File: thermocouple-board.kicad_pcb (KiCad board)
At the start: 2 copper layers, 72 parts, among them J1 Programming Header, J2 RJ45_Amphenol_RJMG1BD3B8K1ANR, J3 Conn_01x02, SW1 RESET, U1 ATSAME51J20A-A, U10 ENC28J60x-SO, U11 MC33063AD, U2 MCP9601_ZM, U3 MCP9601_ZM, U4 MCP9601_ZM, U5 MCP9601_ZM, U6 MCP9601_ZM, U7 MCP9601_ZM, U8 MCP9601_ZM, U9 MCP9601_ZM, Y1 25MHz

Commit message: Begin PCB placement and routing
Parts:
- added J10: TC7, Connector_PinHeader_2.54mm:PinHeader_1x02_P2.54mm_Vertical, F.Cu at (223.6, 71.6)
- added J11: TC8, Connector_PinHeader_2.54mm:PinHeader_1x02_P2.54mm_Vertical, F.Cu at (213.5, 71.6)
- added J4: TC1, Connector_PinHeader_2.54mm:PinHeader_1x02_P2.54mm_Vertical, F.Cu at (284.0, 71.6)
- added J5: TC2, Connector_PinHeader_2.54mm:PinHeader_1x02_P2.54mm_Vertical, F.Cu at (273.9, 71.6)
- added J6: TC3, Connector_PinHeader_2.54mm:PinHeader_1x02_P2.54mm_Vertical, F.Cu at (263.8, 71.6)
- added J7: TC4, Connector_PinHeader_2.54mm:PinHeader_1x02_P2.54mm_Vertical, F.Cu at (253.8, 71.6)
- added J8: TC5, Connector_PinHeader_2.54mm:PinHeader_1x02_P2.54mm_Vertical, F.Cu at (243.7, 71.6)
- added J9: TC6, Connector_PinHeader_2.54mm:PinHeader_1x02_P2.54mm_Vertical, F.Cu at (233.6, 71.6)
- moved J2 253.9 mm to (276.2, 119.4), turned to 90 degrees
- moved C17 246.9 mm to (279.4, 129.5), turned to 90 degrees
- moved C16 230.5 mm to (269.9, 133.3), turned to 90 degrees
- moved Y1 226.2 mm to (252.7, 103.5), turned to 180 degrees
- moved R23 225.4 mm to (285.8, 129.5), turned to 270 degrees
- moved C8 222.0 mm to (266.7, 102.9), turned to 270 degrees
- moved C9 218.5 mm to (263.5, 102.9), turned to 270 degrees
- moved R19 218.2 mm to (269.9, 101.9), turned to 270 degrees
- moved C15 216.2 mm to (273.7, 95.2), turned to 270 degrees
- moved R20 215.2 mm to (273.7, 101.9), turned to 270 degrees
- moved U10 210.9 mm to (255.3, 114.3), turned to 90 degrees
- moved R18 210.8 mm to (269.1, 124.8), turned to 270 degrees
- moved R22 209.9 mm to (264.4, 126.9), turned to 180 degrees
- moved C7 209.9 mm to (259.7, 125.1), turned to 270 degrees
- moved R24 208.1 mm to (278.1, 95.2), turned to 90 degrees
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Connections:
- U2 pad 15: GND -> Net-(U2-Pad15)
- U2 pad 16: (no net) -> GND
- U3 pad 15: /Thermocouples/ADDR_2 -> /Thermocouples/TEST
- U3 pad 16: (no net) -> /Thermocouples/ADDR_2
- U4 pad 15: /Thermocouples/ADDR_3 -> Net-(U4-Pad15)
- U4 pad 16: (no net) -> /Thermocouples/ADDR_3
- U5 pad 15: /Thermocouples/ADDR_4 -> Net-(U5-Pad15)
- U5 pad 16: (no net) -> /Thermocouples/ADDR_4
- U6 pad 15: /Thermocouples/ADDR_5 -> Net-(U6-Pad15)
- U6 pad 16: (no net) -> /Thermocouples/ADDR_5
- U7 pad 16: (no net) -> /Thermocouples/ADDR_6
- U8 pad 15: /Thermocouples/ADDR_7 -> Net-(U8-Pad15)
- U8 pad 16: (no net) -> /Thermocouples/ADDR_7
- U9 pad 15: +3V3 -> Net-(U9-Pad15)
- U9 pad 16: (no net) -> +3V3
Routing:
- net /Thermocouples/SCL: track 0.00 -> 146.2 mm, vias 0 -> 9
- net /Thermocouples/SDA: track 0.00 -> 141.2 mm, vias 0 -> 9
- net +3V3: track 0.00 -> 45.1 mm
- net Net-(R27-Pad2): track 0.00 -> 30.3 mm
- net /MCU/SWDIO: track 0.00 -> 22.0 mm
- net RESET: track 0.00 -> 20.4 mm
- net Net-(C17-Pad2): track 0.00 -> 20.3 mm
- net Net-(J2-PadL2): track 0.00 -> 18.8 mm
- net /Ethernet/TPOUT+: track 0.00 -> 17.8 mm
- net /Ethernet/TPOUT-: track 0.00 -> 12.9 mm
- net Net-(C13-Pad1): track 0.00 -> 12.5 mm
- net Net-(C12-Pad1): track 0.00 -> 12.5 mm
- net Net-(C16-Pad2): track 0.00 -> 10.3 mm
- net Net-(J2-PadL3): track 0.00 -> 9.41 mm
- net /Ethernet/TPIN-: track 0.00 -> 9.14 mm
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
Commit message: Add PDF schematics
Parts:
- J1: footprint Connector_PinSocket_2.54mm:PinSocket_2x05_P2.54mm_Vertical -> Connector_PinHeader_2.54mm:PinHeader_2x05_P2.54mm_Vertical
- moved R32 10.4 mm to (269.9, 146.7), turned to 270 degrees
- moved C18 8.53 mm to (211.7, 123.1), turned to 0 degrees
- moved R26 5.09 mm to (275.0, 142.6)
- moved R19 4.45 mm to (274.3, 101.9)
- moved R20 3.18 mm to (270.5, 101.9)
- moved R14 0.43 mm to (256.3, 125.1)
- moved R15 0.43 mm to (253.8, 125.1)
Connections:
- net /Thermocouples/TC_NEGATIVE_1 renamed /Thermocouples/TC1-
- net /Thermocouples/TC_NEGATIVE_2 renamed /Thermocouples/TC2-
- net /Thermocouples/TC_NEGATIVE_3 renamed /Thermocouples/TC3-
- net /Thermocouples/TC_NEGATIVE_4 renamed /Thermocouples/TC4-
- net /Thermocouples/TC_NEGATIVE_5 renamed /Thermocouples/TC5-
- net /Thermocouples/TC_NEGATIVE_6 renamed /Thermocouples/TC6-
- net /Thermocouples/TC_NEGATIVE_7 renamed /Thermocouples/TC7-
- net /Thermocouples/TC_NEGATIVE_8 renamed /Thermocouples/TC8-
- net /Thermocouples/TC_POSITIVE_1 renamed /Thermocouples/TC1+
- net /Thermocouples/TC_POSITIVE_2 renamed /Thermocouples/TC2+
- net /Thermocouples/TC_POSITIVE_3 renamed /Thermocouples/TC3+
- net /Thermocouples/TC_POSITIVE_4 renamed /Thermocouples/TC4+
- net /Thermocouples/TC_POSITIVE_5 renamed /Thermocouples/TC5+
- net /Thermocouples/TC_POSITIVE_6 renamed /Thermocouples/TC6+
- net /Thermocouples/TC_POSITIVE_7 renamed /Thermocouples/TC7+
- net /Thermocouples/TC_POSITIVE_8 renamed /Thermocouples/TC8+
- net /Thermocouples/TEST renamed Net-(U3-Pad15)
- C20 pad 1: Net-(C20-Pad1) -> +3V3
- J2 pad R5: Net-(J2-PadR5) -> Net-(C16-Pad2)
- L2 pad 2: Net-(C20-Pad1) -> +3V3
- R30 pad 1: Net-(C20-Pad1) -> +3V3
- U2 pad 21: (no net) -> GND
- U3 pad 21: (no net) -> GND
- U4 pad 21: (no net) -> GND
- U5 pad 21: (no net) -> GND
- U6 pad 21: (no net) -> GND
- U7 pad 21: (no net) -> GND
- U8 pad 21: (no net) -> GND
- U9 pad 21: (no net) -> GND
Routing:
- net +3V3: track 45.1 -> 438.4 mm
- net GND: track 0.00 -> 289.1 mm, vias 0 -> 6
- net /Ethernet/LEDA: track 0.00 -> 47.8 mm, vias 0 -> 1
- net /Ethernet/LEDB: track 0.00 -> 41.6 mm
- net /Ethernet/MOSI: track 0.00 -> 39.2 mm, vias 0 -> 2
- net /Ethernet/SCK: track 0.00 -> 38.6 mm, vias 0 -> 2
- net /Ethernet/MISO: track 0.00 -> 36.3 mm, vias 0 -> 2
- net Net-(C15-Pad2): track 0.00 -> 29.9 mm, vias 0 -> 1
- net /MCU/SWCLK: track 0.00 -> 25.7 mm
- net RESET: track 20.4 -> 44.8 mm, vias 0 -> 1
- net Net-(R26-Pad2): track 0.00 -> 24.3 mm
- net VCC: track 0.00 -> 23.2 mm
- net /Ethernet/TPOUT-: track 12.9 -> 34.1 mm, vias 0 -> 2
- net Net-(C16-Pad2): track 10.3 -> 31.0 mm
- net /Ethernet/TPIN-: track 9.14 -> 27.9 mm
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- added copper zone on F.Cu, net GND
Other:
- board outline added: 91.4 x 87.6 mm
- net class Power added: clearance 0.2, trace_width 0.5, via_dia 1, via_drill 0.4
- board text added: "DISOVERY TC PROTOTYPE 1 FEB 2020"
- board text added: "TC1"
- board text added: "TC2"
- board text added: "TC3"
- board text added: "TC4"
- board text added: "TC5"
- board text added: "TC6"
- board text added: "TC7"
- board text added: "TC8"

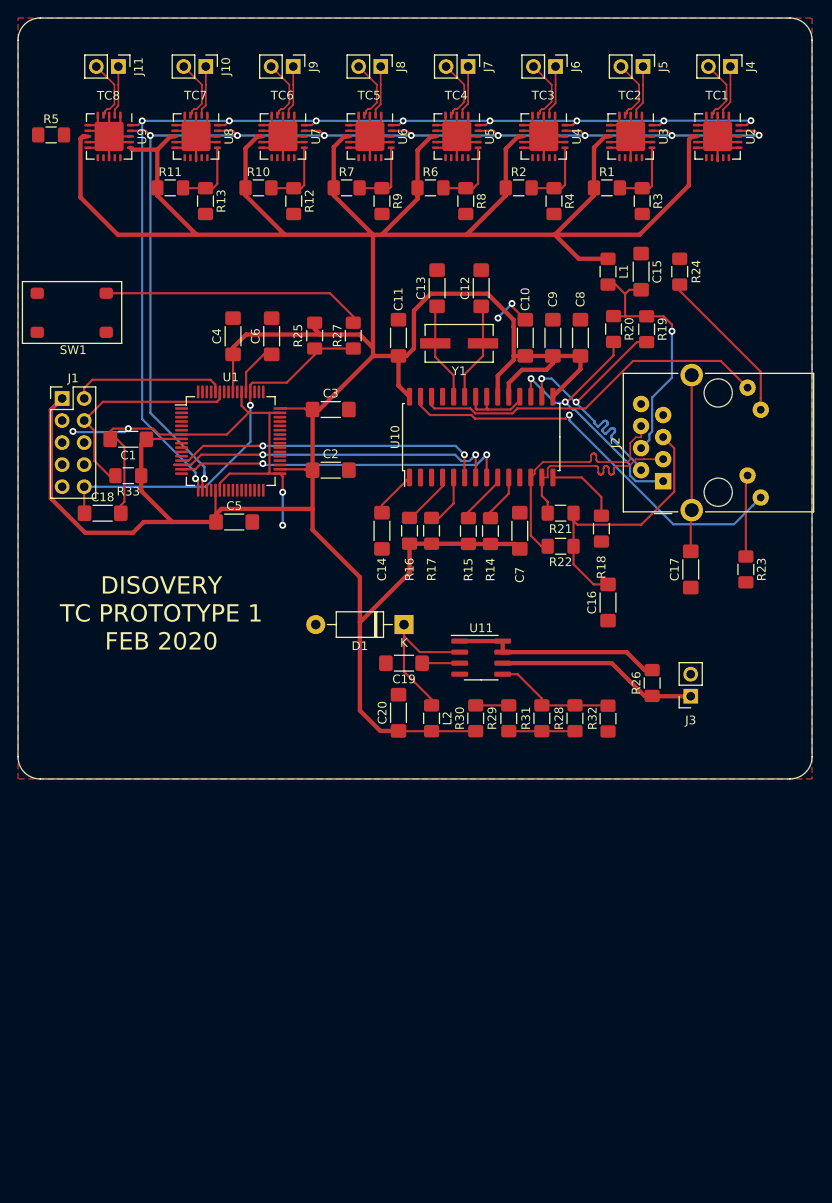
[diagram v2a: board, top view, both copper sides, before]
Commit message: Preliminary replacement of components for MCP9601
Following the changes in the previous commit, all components have been
replaced in a bid for more space efficiency to reduce costs.

No traces have been laid at this point.
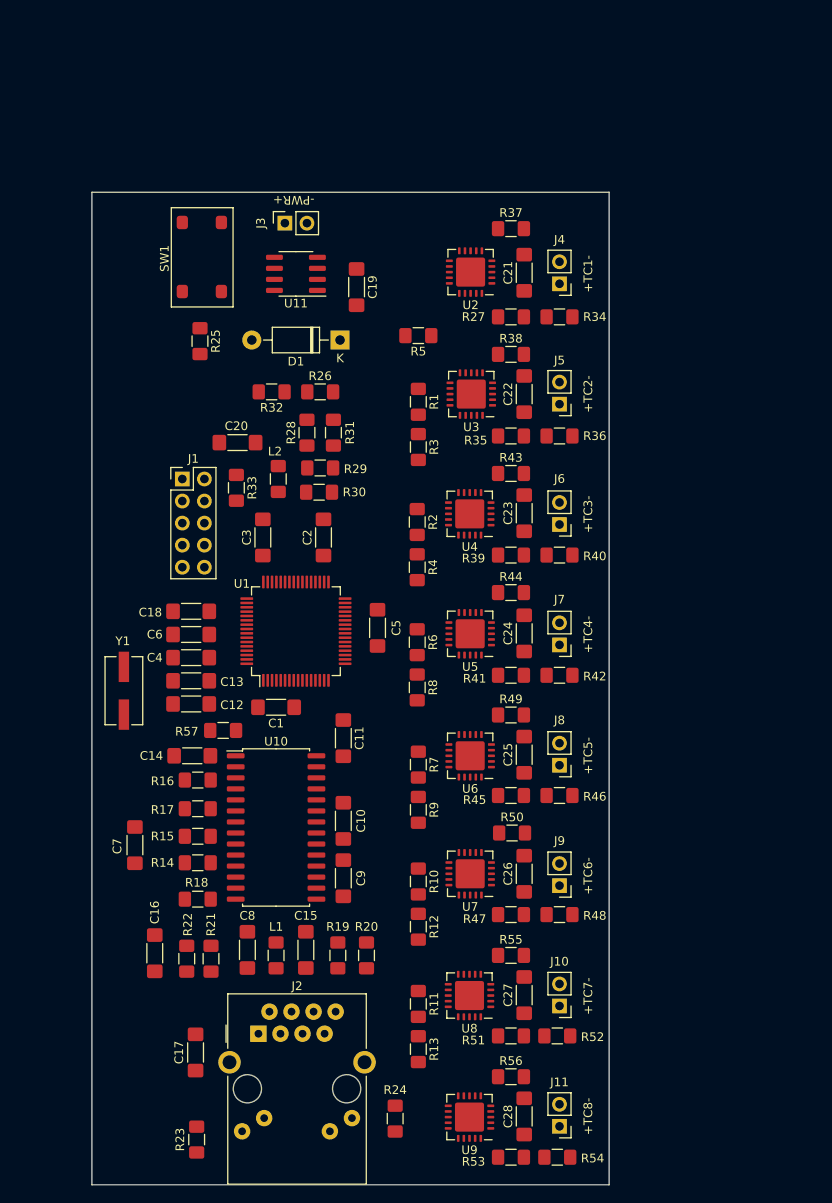
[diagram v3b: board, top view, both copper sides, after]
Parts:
- added C21: 0.1uF, Capacitor_SMD:C_1806_4516Metric_Pad1.57x1.80mm_HandSolder, F.Cu at (260.2, 95.4)
- added C22: 0.1uF, Capacitor_SMD:C_1806_4516Metric_Pad1.57x1.80mm_HandSolder, F.Cu at (260.2, 109.3)
- added C23: 0.1uF, Capacitor_SMD:C_1806_4516Metric_Pad1.57x1.80mm_HandSolder, F.Cu at (260.2, 123.1)
- added C24: 0.1uF, Capacitor_SMD:C_1806_4516Metric_Pad1.57x1.80mm_HandSolder, F.Cu at (260.2, 136.9)
- added C25: 0.1uF, Capacitor_SMD:C_1806_4516Metric_Pad1.57x1.80mm_HandSolder, F.Cu at (260.2, 150.9)
- added C26: 0.1uF, Capacitor_SMD:C_1806_4516Metric_Pad1.57x1.80mm_HandSolder, F.Cu at (260.2, 164.6)
- added C27: 0.1uF, Capacitor_SMD:C_1806_4516Metric_Pad1.57x1.80mm_HandSolder, F.Cu at (260.2, 178.6)
- added C28: 0.1uF, Capacitor_SMD:C_1806_4516Metric_Pad1.57x1.80mm_HandSolder, F.Cu at (260.2, 192.5)
- added R34: 1M, Resistor_SMD:R_1206_3216Metric_Pad1.42x1.75mm_HandSolder, F.Cu at (264.3, 100.5)
- added R35: 2M, Resistor_SMD:R_1206_3216Metric_Pad1.42x1.75mm_HandSolder, F.Cu at (258.7, 114.2)
- added R36: 1M, Resistor_SMD:R_1206_3216Metric_Pad1.42x1.75mm_HandSolder, F.Cu at (264.3, 114.2)
- added R37: 2M, Resistor_SMD:R_1206_3216Metric_Pad1.42x1.75mm_HandSolder, F.Cu at (258.7, 90.3)
- added R38: 2M, Resistor_SMD:R_1206_3216Metric_Pad1.42x1.75mm_HandSolder, F.Cu at (258.7, 104.8)
- added R39: 2M, Resistor_SMD:R_1206_3216Metric_Pad1.42x1.75mm_HandSolder, F.Cu at (258.7, 127.9)
- added R40: 1M, Resistor_SMD:R_1206_3216Metric_Pad1.42x1.75mm_HandSolder, F.Cu at (264.3, 127.9)
- added R41: 2M, Resistor_SMD:R_1206_3216Metric_Pad1.42x1.75mm_HandSolder, F.Cu at (258.7, 141.7)
- added R42: 1M, Resistor_SMD:R_1206_3216Metric_Pad1.42x1.75mm_HandSolder, F.Cu at (264.3, 141.7)
- added R43: 2M, Resistor_SMD:R_1206_3216Metric_Pad1.42x1.75mm_HandSolder, F.Cu at (258.7, 118.5)
- added R44: 2M, Resistor_SMD:R_1206_3216Metric_Pad1.42x1.75mm_HandSolder, F.Cu at (258.7, 132.2)
- added R45: 2M, Resistor_SMD:R_1206_3216Metric_Pad1.42x1.75mm_HandSolder, F.Cu at (258.7, 155.6)
- added R46: 1M, Resistor_SMD:R_1206_3216Metric_Pad1.42x1.75mm_HandSolder, F.Cu at (264.3, 155.6)
- added R47: 2M, Resistor_SMD:R_1206_3216Metric_Pad1.42x1.75mm_HandSolder, F.Cu at (258.7, 169.3)
- added R48: 1M, Resistor_SMD:R_1206_3216Metric_Pad1.42x1.75mm_HandSolder, F.Cu at (264.3, 169.3)
- added R49: 2M, Resistor_SMD:R_1206_3216Metric_Pad1.42x1.75mm_HandSolder, F.Cu at (258.7, 146.3)
- added R50: 2M, Resistor_SMD:R_1206_3216Metric_Pad1.42x1.75mm_HandSolder, F.Cu at (258.8, 159.9)
- added R51: 2M, Resistor_SMD:R_1206_3216Metric_Pad1.42x1.75mm_HandSolder, F.Cu at (258.7, 183.3)
- added R52: 1M, Resistor_SMD:R_1206_3216Metric_Pad1.42x1.75mm_HandSolder, F.Cu at (264.0, 183.3)
- added R53: 2M, Resistor_SMD:R_1206_3216Metric_Pad1.42x1.75mm_HandSolder, F.Cu at (258.7, 197.2)
- added R54: 1M, Resistor_SMD:R_1206_3216Metric_Pad1.42x1.75mm_HandSolder, F.Cu at (264.0, 197.2)
- added R55: 2M, Resistor_SMD:R_1206_3216Metric_Pad1.42x1.75mm_HandSolder, F.Cu at (258.7, 174.0)
- added R56: 2M, Resistor_SMD:R_1206_3216Metric_Pad1.42x1.75mm_HandSolder, F.Cu at (258.7, 188.0)
- added R57: 5M, Resistor_SMD:R_1206_3216Metric_Pad1.42x1.75mm_HandSolder, F.Cu at (225.6, 148.1)
- R25: value 27K -> 330
- R27: value 820 -> 2M
- R33: value 4.7K -> 1K
- moved J11 132.2 mm to (264.3, 193.7), turned to 180 degrees
- moved U9 120.3 mm to (253.9, 192.6), turned to 180 degrees
- moved J10 115.6 mm to (264.3, 179.8), turned to 180 degrees
- moved U8 103.8 mm to (253.9, 178.6), turned to 180 degrees
- moved R24 102.9 mm to (245.4, 192.8)
- moved R13 100.7 mm to (248.0, 184.8)
- moved J9 99.2 mm to (264.3, 166.0), turned to 180 degrees
- moved R11 98.2 mm to (248.0, 179.6), turned to 270 degrees
- moved R23 91.2 mm to (222.5, 195.2)
- moved U7 87.6 mm to (254.0, 164.6), turned to 180 degrees
- moved L1 87.5 mm to (231.6, 174.0)
- moved C15 87.1 mm to (235.1, 173.4)
- moved R12 84.8 mm to (248.0, 170.7)
- moved J8 83.1 mm to (264.3, 152.1), turned to 180 degrees
- moved R10 82.0 mm to (248.0, 165.5), turned to 270 degrees
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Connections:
- C18 pad 1: RESET -> +3V3
- J1 pad 10: RESET -> +3V3
- J2 pad R3: /Ethernet/TPIN+ -> Net-(C16-Pad2)
- J2 pad R5: Net-(C16-Pad2) -> Net-(J2-PadR5)
- J2 pad R6: /Ethernet/TPIN- -> Net-(C16-Pad2)
- R21 pad 1: Net-(C16-Pad2) -> /Ethernet/TPIN+
- R21 pad 2: /Ethernet/TPIN+ -> Net-(C16-Pad2)
- R22 pad 1: Net-(C16-Pad2) -> /Ethernet/TPIN-
- R22 pad 2: /Ethernet/TPIN- -> Net-(C16-Pad2)
- R25 pad 1: +3V3 -> Net-(R25-Pad1)
- R25 pad 2: RESET -> +3V3
- R27 pad 1: RESET -> GND
- R27 pad 2: Net-(R27-Pad2) -> /Thermocouples/TC1+
- R5 pad 1: +5V -> +3V3
- SW1 pad 1: GND -> Net-(R25-Pad1)
- SW1 pad 2: Net-(R27-Pad2) -> GND
- U1 pad 52: RESET -> +3V3
- U10 pad 24: Net-(C13-Pad1) -> Net-(R57-Pad1)
- U10 pad 25: Net-(U10-Pad25) -> +3V3
- U2 pad 6: GND -> /Thermocouples/TC1+
- U2 pad 7: GND -> Net-(U2-Pad7)
- U2 pad 9: GND -> Net-(U2-Pad9)
- U3 pad 6: GND -> /Thermocouples/TC2+
- U3 pad 7: GND -> Net-(U3-Pad7)
- U3 pad 9: GND -> Net-(U3-Pad9)
- U4 pad 6: GND -> /Thermocouples/TC3+
- U4 pad 7: GND -> Net-(U4-Pad7)
- U4 pad 9: GND -> Net-(U4-Pad9)
- U5 pad 6: GND -> /Thermocouples/TC4+
- U5 pad 7: GND -> Net-(U5-Pad7)
- U5 pad 9: GND -> Net-(U5-Pad9)
- U6 pad 6: GND -> /Thermocouples/TC5+
- U6 pad 7: GND -> Net-(U6-Pad7)
- U6 pad 9: GND -> Net-(U6-Pad9)
- U7 pad 6: GND -> /Thermocouples/TC6+
- U7 pad 7: GND -> Net-(U7-Pad7)
- U7 pad 9: GND -> Net-(U7-Pad9)
- U8 pad 6: GND -> /Thermocouples/TC7+
- U8 pad 7: GND -> Net-(U8-Pad7)
- U8 pad 9: GND -> Net-(U8-Pad9)
- U9 pad 6: GND -> /Thermocouples/TC8+
- U9 pad 7: GND -> Net-(U9-Pad7)
- U9 pad 9: GND -> Net-(U9-Pad9)
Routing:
- net +3V3: track 438.4 -> 0.00 mm
- net GND: track 289.1 -> 0.00 mm, vias 6 -> 0
- net /Thermocouples/SCL: track 134.3 -> 0.00 mm, vias 9 -> 0
- net /Thermocouples/SDA: track 128.2 -> 0.00 mm, vias 9 -> 0
- net /Ethernet/LEDA: track 47.8 -> 0.00 mm, vias 1 -> 0
- net RESET: track 44.8 -> 0.00 mm, vias 1 -> 0
- net /Ethernet/LEDB: track 41.6 -> 0.00 mm
- net /Ethernet/MOSI: track 39.2 -> 0.00 mm, vias 2 -> 0
- net /Ethernet/SCK: track 38.6 -> 0.00 mm, vias 2 -> 0
- net /Ethernet/MISO: track 36.3 -> 0.00 mm, vias 2 -> 0
- net /Ethernet/TPOUT-: track 34.1 -> 0.00 mm, vias 2 -> 0
- net /Ethernet/TPOUT+: track 32.2 -> 0.00 mm, vias 2 -> 0
- net Net-(C16-Pad2): track 31.0 -> 0.00 mm
- net Net-(R27-Pad2): track 30.3 -> 0.00 mm
- net Net-(C15-Pad2): track 29.9 -> 0.00 mm, vias 1 -> 0
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- removed copper zone on F.Cu, net GND
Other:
- board size 91.4 x 87.6 mm -> 59.6 x 114.3 mm
- board text added: "+TC1-"
- board text added: "+TC2-"
- board text added: "+TC3-"
- board text added: "+TC4-"
- board text added: "+TC5-"
- board text added: "+TC6-"
- board text added: "+TC7-"
- board text added: "+TC8-"
- board text added: "-PWR+"
- board text removed: "DISOVERY TC PROTOTYPE 1 FEB 2020"
- board text removed: "TC1"
- board text removed: "TC2"
- board text removed: "TC3"
- board text removed: "TC4"
- board text removed: "TC5"
- board text removed: "TC6"
- board text removed: "TC7"
- board text removed: "TC8"

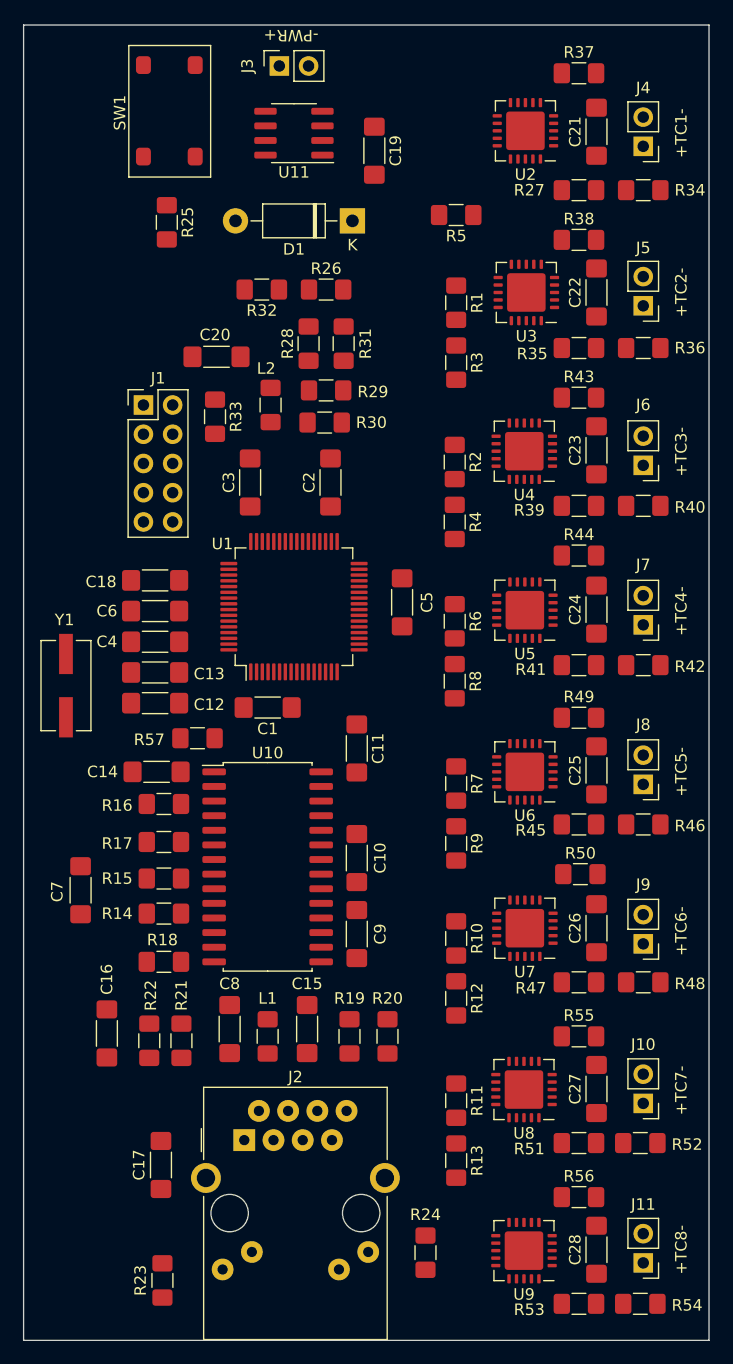
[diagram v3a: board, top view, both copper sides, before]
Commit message: Complete routing for PCB traces
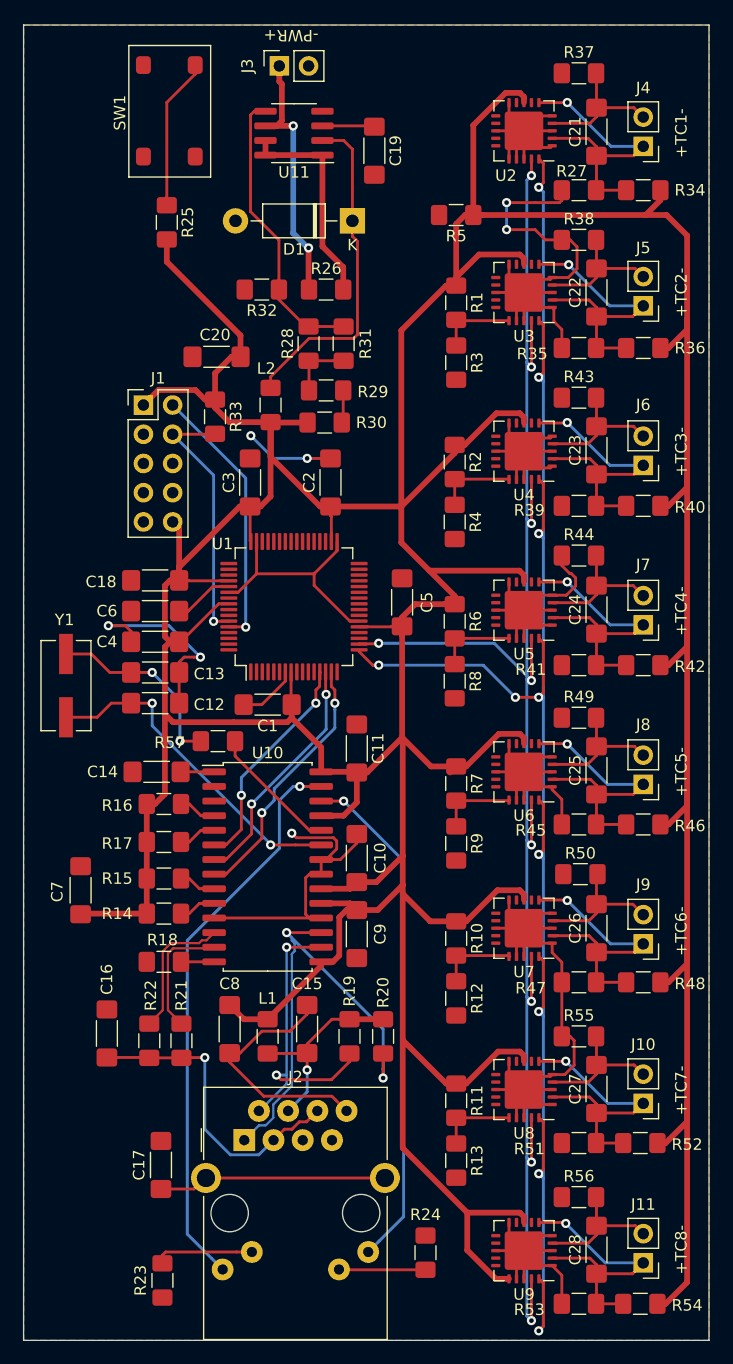
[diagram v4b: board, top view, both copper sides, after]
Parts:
- moved R57 1.80 mm to (227.3, 148.3)
- moved R20 0.38 mm to (241.7, 174.0), turned to 270 degrees
- moved C1 0.25 mm to (231.6, 145.2)
- moved U3 0.21 mm to (253.9, 109.3)
- moved U2 0.13 mm to (253.9, 95.3)
- moved U5 0.08 mm to (253.9, 137.0)
- moved U6 0.08 mm to (253.9, 151.0)
- moved U7 0.08 mm to (253.9, 164.6)
- turned R19 to 270 degrees
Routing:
- net +3V3: track 0.00 -> 543.7 mm
- net GND: track 0.00 -> 306.5 mm, vias 0 -> 7
- net /Thermocouples/SDA: track 0.00 -> 159.7 mm, vias 0 -> 10
- net /Thermocouples/SCL: track 0.00 -> 148.1 mm, vias 0 -> 9
- net /Ethernet/LEDA: track 0.00 -> 49.5 mm, vias 0 -> 1
- net /Ethernet/LEDB: track 0.00 -> 44.6 mm, vias 0 -> 1
- net /Ethernet/TPOUT+: track 0.00 -> 41.7 mm, vias 0 -> 2
- net Net-(D1-Pad1): track 0.00 -> 29.2 mm
- net Net-(C12-Pad1): track 0.00 -> 29.0 mm, vias 0 -> 2
- net /Ethernet/TPOUT-: track 0.00 -> 27.3 mm, vias 0 -> 2
- net Net-(C16-Pad2): track 0.00 -> 27.0 mm, vias 0 -> 1
- net /Thermocouples/TC3+: track 0.00 -> 25.7 mm, vias 0 -> 1
- net /Thermocouples/TC4+: track 0.00 -> 25.7 mm, vias 0 -> 1
- net /Thermocouples/TC6+: track 0.00 -> 25.6 mm, vias 0 -> 1
- net /Thermocouples/TC5+: track 0.00 -> 25.5 mm, vias 0 -> 1
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- added copper zone on F.Cu, net GND
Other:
- net class Power: trace_width 0.5 -> 0.25
